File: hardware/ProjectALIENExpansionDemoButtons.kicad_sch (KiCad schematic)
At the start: 8 parts, among them J1 Excess GPIO Pins, J2 Voltage Breakout

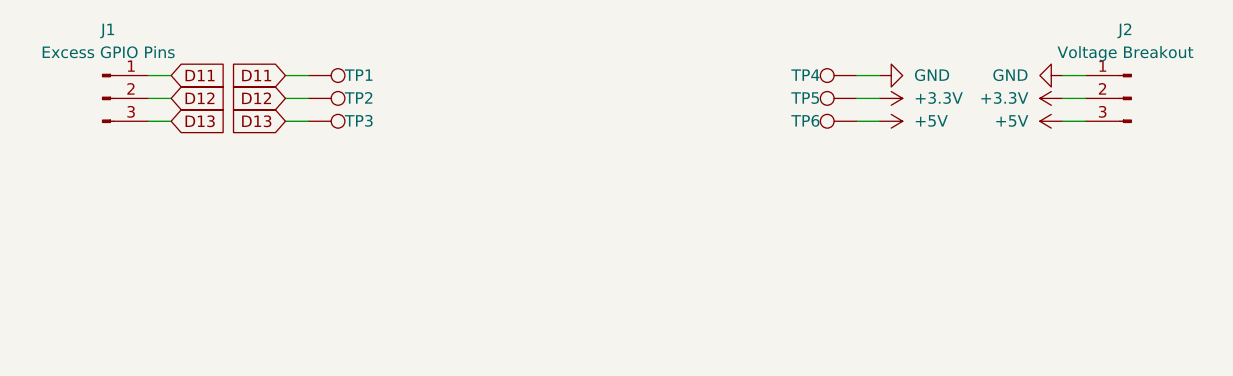
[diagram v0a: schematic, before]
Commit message: Wired up buttons
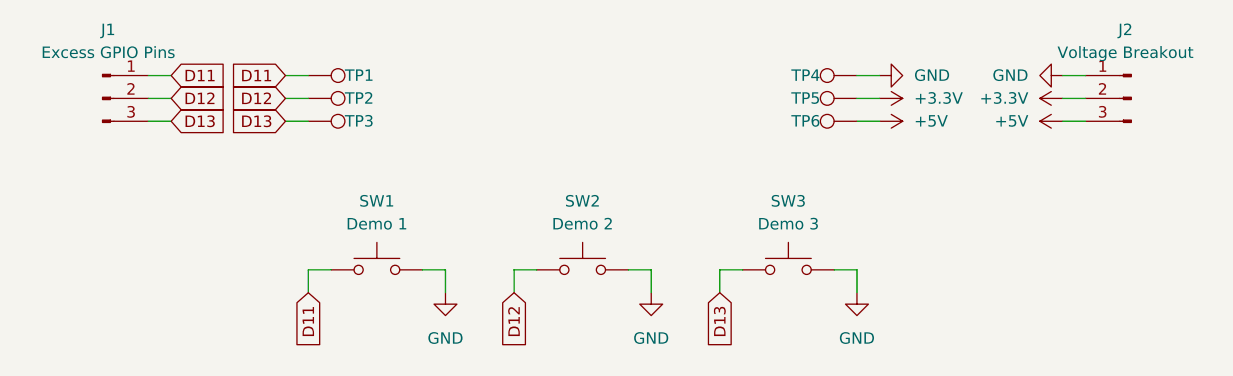
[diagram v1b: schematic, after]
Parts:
- added SW1: Demo 1, Two_Pin_Through_Hole_Push_Button:Two_Pin_Through_Hole_Push_Button, symbol Switch:SW_Push
- added SW2: Demo 2, Two_Pin_Through_Hole_Push_Button:Two_Pin_Through_Hole_Push_Button, symbol Switch:SW_Push
- added SW3: Demo 3, Two_Pin_Through_Hole_Push_Button:Two_Pin_Through_Hole_Push_Button, symbol Switch:SW_Push
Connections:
- net D11: now also SW1.1
- net D12: now also SW2.1
- net D13: now also SW3.1
- net GND: now also SW1.2, SW2.2, SW3.2
